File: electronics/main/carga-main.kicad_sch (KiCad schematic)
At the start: 74 parts, among them J1 USB2UART, J2 1.47 IPS LCD, J3 ConnBattery, J4 RTD_PT100, Q1 SS8050, Q2 SS8050, Q3 SS8050, SW1 RST, SW2 IN1, SW3 Boot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

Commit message: feat: add voltage regulator to carga main
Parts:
- removed C12, C18, C19, C20: 100nF, Capacitor_SMD:C_0805_2012Metric_Pad1.18x1.45mm_HandSolder, symbol Device:C
- removed C13, C16, C17: 10uF, Capacitor_SMD:C_0805_2012Metric_Pad1.18x1.45mm_HandSolder, symbol Device:C
- removed C22, C23: 4.7uF, Capacitor_SMD:C_0805_2012Metric_Pad1.18x1.45mm_HandSolder, symbol Device:C
- removed D1: INDICATOR, LED_SMD:LED_1206_3216Metric_Pad1.42x1.75mm_HandSolder, symbol Device:LED
- removed D2: VDD, LED_SMD:LED_1206_3216Metric_Pad1.42x1.75mm_HandSolder, symbol Device:LED
- removed D4: red, LED_SMD:LED_0805_2012Metric_Pad1.15x1.40mm_HandSolder, symbol Device:LED
- removed J3: ConnBattery, Connector_PinHeader_2.54mm:PinHeader_1x03_P2.54mm_Vertical, symbol Connector_Generic:Conn_01x03
- removed J4: RTD_PT100, TerminalBlock_Phoenix:TerminalBlock_Phoenix_PT-1,5-3-5.0-H_1x03_P5.00mm_Horizontal, symbol Connector:Screw_Terminal_01x03
- removed JP1: 3_OR_2_Wire, Jumper:SolderJumper-3_P1.3mm_Open_RoundedPad1.0x1.5mm, symbol Jumper:SolderJumper_3_Open
- removed JP2: 2_Wire, Jumper:SolderJumper-2_P1.3mm_Open_TrianglePad1.0x1.5mm, symbol Jumper:SolderJumper_2_Open
- removed L1: 22uH 1A, Inductor_SMD:L_Bourns_SRP7028A_7.3x6.6mm, symbol Device:L
- removed Q3: SS8050, Package_TO_SOT_SMD:SOT-23_Handsoldering, symbol Transistor_BJT:BC817
- removed R13, R14: 1k, Resistor_SMD:R_0805_2012Metric_Pad1.20x1.40mm_HandSolder, symbol Device:R_US
- removed R15: 100, Resistor_SMD:R_0805_2012Metric_Pad1.20x1.40mm_HandSolder, symbol Device:R_US
- removed R16: 46.4K, Resistor_SMD:R_0805_2012Metric_Pad1.20x1.40mm_HandSolder, symbol Device:R_US
- removed R17: 2K2, Resistor_SMD:R_0805_2012Metric_Pad1.20x1.40mm_HandSolder, symbol Device:R_US
- removed R18: 1.13k, Resistor_SMD:R_0805_2012Metric_Pad1.20x1.40mm_HandSolder, symbol Device:R_US
- removed R19: 400 1%, Resistor_SMD:R_0805_2012Metric_Pad1.20x1.40mm_HandSolder, symbol Device:R_US
- removed R20, R21: 1K5, Resistor_SMD:R_0805_2012Metric_Pad1.20x1.40mm_HandSolder, symbol Device:R_US
- removed U3: TPS63001_SEPIC_3V3, Package_SON:Texas_DRC0010J_ThermalVias, symbol Regulator_Switching:TPS63001
- removed U4: MAX31865xTP, Package_DFN_QFN:TQFN-20-1EP_5x5mm_P0.65mm_EP3.25x3.25mm, symbol Sensor_Temperature:MAX31865xTP
- removed U5: BQ24075RGT_DPPM, Package_DFN_QFN:VQFN-16-1EP_3x3mm_P0.5mm_EP1.6x1.6mm, symbol Battery_Management:BQ24075RGT
- removed U6: HX711, Package_SO:SOIC-16_3.9x9.9mm_P1.27mm, symbol Analog_ADC:HX711
- added C12: 0.33uF, Capacitor_SMD:C_0805_2012Metric_Pad1.18x1.45mm_HandSolder, symbol Device:C_Polarized
- added C13: 0.1uF, Capacitor_SMD:C_0805_2012Metric_Pad1.18x1.45mm_HandSolder, symbol Device:C_Polarized
- added J12: PWRInput, TerminalBlock_Phoenix:TerminalBlock_Phoenix_PT-1,5-2-5.0-H_1x02_P5.00mm_Horizontal, symbol Connector:Screw_Terminal_01x02
- added J4: DriverConn2, Connector_IDC:IDC-Header_2x05_P2.54mm_Vertical, symbol Connector_Generic:Conn_02x05_Odd_Even
- added J5: DriverConn, Connector_IDC:IDC-Header_2x05_P2.54mm_Vertical, symbol Connector_Generic:Conn_02x05_Odd_Even
- added J6: SensorConn, Connector_IDC:IDC-Header_2x05_P2.54mm_Vertical, symbol Connector_Generic:Conn_02x05_Odd_Even
- added U3: L7805, Package_TO_SOT_THT:TO-220F-3_Horizontal_TabDown, symbol Regulator_Linear:L7805
- added U4: AMS1117-3.3, Package_TO_SOT_SMD:SOT-223-3_TabPin2, symbol Regulator_Linear:AMS1117-3.3
- C14: value 0.1uF -> 22uF
- C15: value 1uF -> 22uF
- D3: value green -> PWR; footprint LED_SMD:LED_0805_2012Metric_Pad1.15x1.40mm_HandSolder -> LED_SMD:LED_1206_3216Metric_Pad1.42x1.75mm_HandSolder
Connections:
- net ~{PGOOD} is gone; now on net GND: D3.1 (K)
- net +3.3V: now also C15.1, J5.1 (Pin_1), J6.1 (Pin_1), U4.2 (VO)
- net GND: now also C12.2, C13.2, J12.2 (Pin_2), J5.10 (Pin_10), J6.10 (Pin_10), U3.2 (GND), U4.1 (GND)
- net VBUS: no longer C15.1
- net at D3.2 (A): now also R8.2
- net +5V: now reaches R8.1
- net +5V: now also C14.1, C13.1, J5.2 (Pin_2), J6.2 (Pin_2), U3.3 (OUT), U4.3 (VI)
- net at U2.4 (IO4): no longer R8.2
- net IN_SOL_VIB: now reaches U2.16 (IO46)
- net IN_SOL_VIB: now also J4.7 (Pin_7)
- net IN_SOL_VIA: now reaches U2.26 (IO45)
- net IN_SOL_VIA: now also J4.5 (Pin_5)
- net IN_ENA1: now reaches U2.31 (IO38)
- net IN_ENA1: now also J5.3 (Pin_3)
- net IN_ENB1: now reaches U2.32 (IO39)
- net IN_ENB1: now also J5.5 (Pin_5)
- net IN_ENA2: now reaches U2.33 (IO40)
- net IN_ENA2: now also J5.7 (Pin_7)
- net IN_ENB2: now reaches U2.34 (IO41)
- net IN_ENB2: now also J5.9 (Pin_9)
- net IN_SERVO: now reaches U2.35 (IO42)
- net IN_SERVO: now also J4.3 (Pin_3)
- net PD_SCK: now reaches U2.38 (IO2)
- net PD_SCK: now also J6.6 (Pin_6)
- net DOUT: now reaches U2.39 (IO1)
- net DOUT: now also J6.4 (Pin_4)
- net I2C_SDA: now reaches U2.6 (IO6)
- net I2C_SDA: now also J5.6 (Pin_6)
- net I2C_SCK: now reaches U2.7 (IO7)
- net I2C_SCK: now also J5.8 (Pin_8)
- new net +12V: C12.1, J12.1 (Pin_1), U3.1 (IN)
- new net GNDA: J4.10 (Pin_10)
- new net GNDB: J4.8 (Pin_8)
- new net VDDA: J4.2 (Pin_2)
- new net VDDB: J4.4 (Pin_4)
- new net VM: J5.4 (Pin_4)
- new net VSER: J4.1 (Pin_1)
- no-connect marks 24 -> 11
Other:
- note removed: "3 Wire to Force+ 2/4 Wire to GND Connect 2_Wire if use 2/4 Wire"
- note removed: "DPPM"
- note removed: "Program Fast-Charge Safety Timer (TMR): RTMR = tMAXCHG / (10 × KTMR ) KTMR = 48 s/kΩ from the electrical characteristics table. RTMR = (6.25 hr × 3600 s/hr) / (10 × 48 s/kΩ) = 46.8 kΩ -> 46.4 kΩ"
- note removed: "Program the Fast Charge Current (ISET): RISET = KISET / ICHG KISET = 890 AΩ from the electrical characteristics table. RISET = 890 AΩ / 0.8 A = 1.1125 kΩ -> 1.13 kΩ"
- note removed: "SEPIC 3.3V"
- note removed: "dynamic power path management"
- title: (none) -> Carga Main Module
- moved on the sheet: C1, C10, C11, C2, C3, C4, C5, C6, C7, C8, C9, H1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

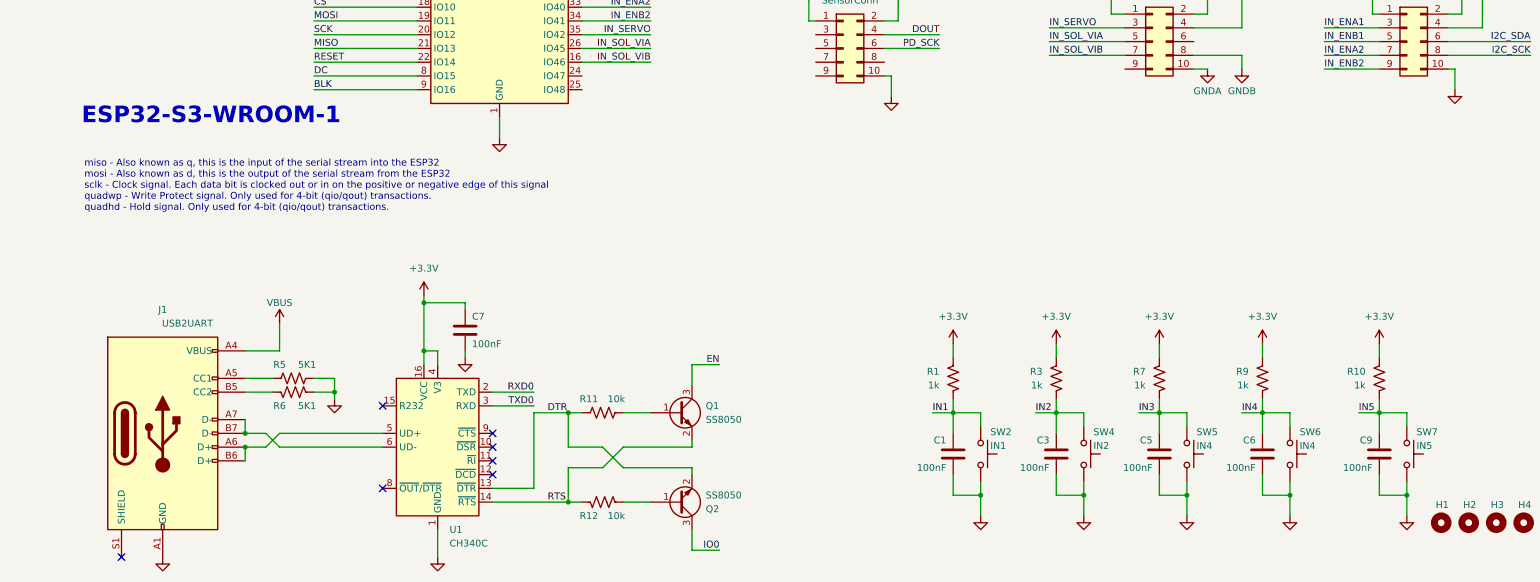
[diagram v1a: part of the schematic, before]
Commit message: feat: arrange component in carga main
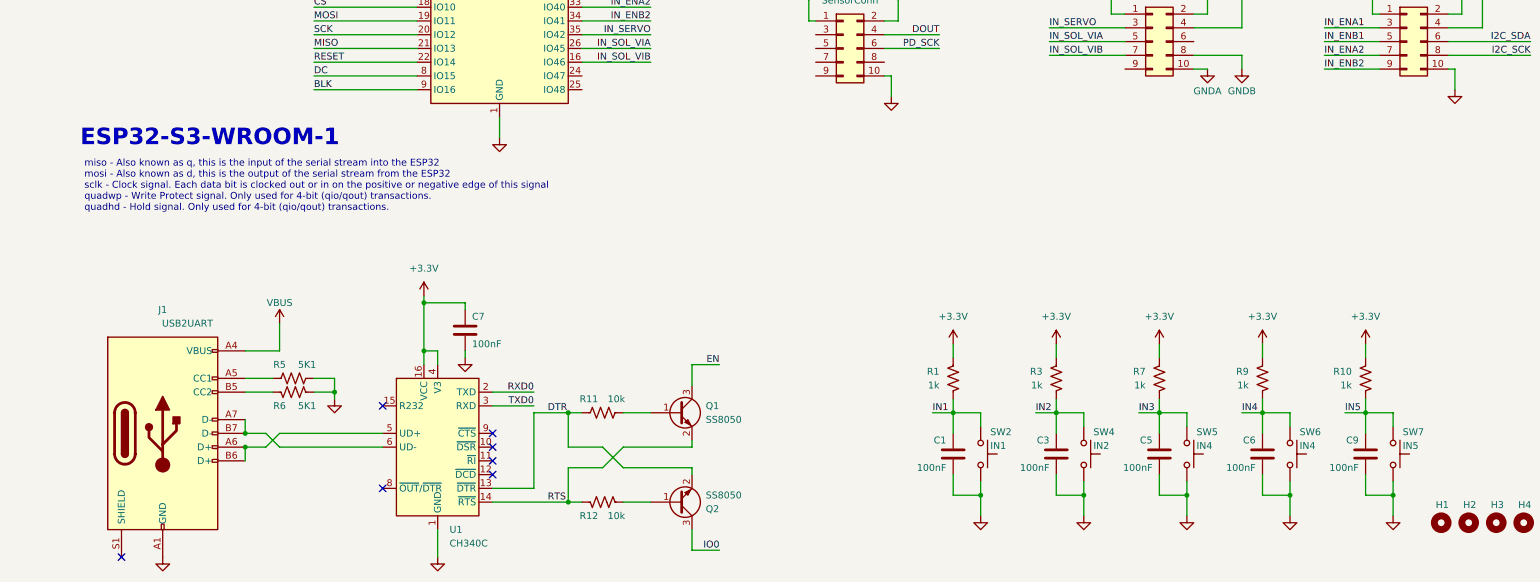
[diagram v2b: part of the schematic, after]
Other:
- moved on the sheet: C9, R10, SW7
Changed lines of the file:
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@@
 	(text "ESP32-S3-WROOM-1"
 		(exclude_from_sim no)
-		(at 14.224 85.598 0)
+		(at 13.97 89.662 0)
 		(effects
 			(font
@@
 	)
 	(junction
-		(at 254 142.24)
+		(at 251.46 142.24)
 		(diameter 0)
 		(color 0 0 0 0)
@@
 	)
 	(junction
-		(at 259.08 157.48)
+		(at 256.54 157.48)
 		(diameter 0)
 		(color 0 0 0 0)
@@
 	(wire
 		(pts
-			(xy 259.08 154.94) (xy 259.08 157.48)
+			(xy 256.54 154.94) (xy 256.54 157.48)
 		)
 		(stroke
@@
 	(wire
 		(pts
-			(xy 259.08 142.24) (xy 254 142.24)
+			(xy 256.54 142.24) (xy 251.46 142.24)
 		)
 		(stroke
@@
 	(wire
 		(pts
-			(xy 259.08 157.48) (xy 254 157.48)
+			(xy 256.54 157.48) (xy 251.46 157.48)
 		)
 		(stroke
@@
 	(wire
 		(pts
-			(xy 254 142.24) (xy 254 146.05)
+			(xy 251.46 142.24) (xy 251.46 146.05)
 		)
 		(stroke
@@
 	(wire
 		(pts
-			(xy 254 139.7) (xy 254 142.24)
+			(xy 251.46 139.7) (xy 251.46 142.24)
 		)
 		(stroke
@@
 	(wire
 		(pts
-			(xy 259.08 144.78) (xy 259.08 142.24)
+			(xy 256.54 144.78) (xy 256.54 142.24)
 		)
 		(stroke
@@
 	(wire
 		(pts
-			(xy 259.08 157.48) (xy 259.08 161.29)
+			(xy 256.54 157.48) (xy 256.54 161.29)
 		)
 		(stroke
@@
 	(wire
 		(pts
-			(xy 254 129.54) (xy 254 132.08)
+			(xy 251.46 129.54) (xy 251.46 132.08)
 		)
 		(stroke
@@
 	(wire
 		(pts
-			(xy 250.19 142.24) (xy 254 142.24)
+			(xy 247.65 142.24) (xy 251.46 142.24)
 		)
 		(stroke
@@
 	(wire
 		(pts
-			(xy 254 157.48) (xy 254 153.67)
+			(xy 251.46 157.48) (xy 251.46 153.67)
 		)
 		(stroke
@@
 	)
 	(label "IN5"
-		(at 250.19 142.24 0)
+		(at 247.65 142.24 0)
 		(effects
 			(font
@@
 	(symbol
 		(lib_id "Device:C")
-		(at 254 149.86 0)
+		(at 251.46 149.86 0)
 		(mirror y)
 		(unit 1)
@@
 		(dnp no)
 		(property "Reference" "C9"
-			(at 252.73 147.32 0)
+			(at 250.19 147.32 0)
 			(effects
 				(font
@@
 		)
 		(property "Value" "100nF"
-			(at 252.73 152.4 0)
+			(at 250.19 152.4 0)
 			(effects
 				(font
@@
 		)
 		(property "Footprint" "Capacitor_SMD:C_0805_2012Metric_Pad1.18x1.45mm_HandSolder"
-			(at 253.0348 153.67 0)
+			(at 250.4948 153.67 0)
 			(effects
 				(font
@@
 		)
 		(property "Datasheet" "~"
-			(at 254 149.86 0)
+			(at 251.46 149.86 0)
 			(effects
 				(font
@@
 		)
 		(property "Description" ""
-			(at 254 149.86 0)
+			(at 251.46 149.86 0)
 			(effects
 				(font
@@
 	(symbol
 		(lib_id "power:GND")
-		(at 259.08 161.29 0)
+		(at 256.54 161.29 0)
 		(mirror y)
 		(unit 1)
@@
 		(dnp no)
 		(property "Reference" "#PWR023"
-			(at 259.08 167.64 0)
+			(at 256.54 167.64 0)
 			(effects
 				(font
@@
 		)
 		(property "Value" "GND"
-			(at 261.62 163.83 0)
+			(at 259.08 163.83 0)
 			(effects
 				(font
@@
 		)
 		(property "Footprint" ""
-			(at 259.08 161.29 0)
+			(at 256.54 161.29 0)
 			(effects
 				(font
@@
 		)
 		(property "Datasheet" ""
-			(at 259.08 161.29 0)
+			(at 256.54 161.29 0)
 			(effects
 				(font
@@
 		)
 		(property "Description" ""
-			(at 259.08 161.29 0)
+			(at 256.54 161.29 0)
 			(effects
 				(font
@@
 		(on_board yes)
 		(dnp no)
-		(property "Reference" "#PWR025"
+		(property "Reference" "#PWR0101"
 			(at 222.25 85.09 0)
 			(effects
@@
 			(project "carga-main"
 				(path "/11d31181-5c23-445f-b117-2be40d0a6fe8"
-					(reference "#PWR025")
+					(reference "#PWR0101")
 					(unit 1)
 				)
@@
 		(dnp no)
 		(fields_autoplaced yes)
-		(property "Reference" "#PWR026"
+		(property "Reference" "#PWR0102"
 			(at 273.05 68.58 0)
 			(effects
@@
 			(project "carga-main"
 				(path "/11d31181-5c23-445f-b117-2be40d0a6fe8"
-					(reference "#PWR026")
+					(reference "#PWR0102")
 					(unit 1)
 				)
@@
 	(symbol
 		(lib_id "Switch:SW_Push")
-		(at 259.08 149.86 270)
+		(at 256.54 149.86 270)
 		(mirror x)
 		(unit 1)
@@
 		(dnp no)
 		(property "Reference" "SW7"
-			(at 260.858 145.796 90)
+			(at 258.318 145.796 90)
 			(effects
 				(font
@@
 		)
 		(property "Value" "IN5"
-			(at 260.858 148.336 90)
+			(at 258.318 148.336 90)
 			(effects
 				(font
@@
 		)
 		(property "Footprint" "Button_Switch_SMD:SW_SPST_Omron_B3FS-100xP"
-			(at 264.16 149.86 0)
+			(at 261.62 149.86 0)
 			(effects
 				(font
@@
 		)
 		(property "Datasheet" "~"
-			(at 264.16 149.86 0)
+			(at 261.62 149.86 0)
 			(effects
 				(font
@@
 		)
 		(property "Description" "Push button switch, generic, two pins"
-			(at 259.08 149.86 0)
+			(at 256.54 149.86 0)
 			(effects
 				(font
@@
 	(symbol
 		(lib_id "Device:R_US")
-		(at 254 135.89 0)
+		(at 251.46 135.89 0)
 		(mirror y)
 		(unit 1)
@@
 		(dnp no)
 		(property "Reference" "R10"
-			(at 251.46 134.6199 0)
+			(at 248.92 134.6199 0)
 			(effects
 				(font
@@
 		)
 		(property "Value" "1k"
-			(at 251.46 137.1599 0)
+			(at 248.92 137.1599 0)
 			(effects
 				(font
@@
 		)
 		(property "Footprint" "Resistor_SMD:R_0805_2012Metric_Pad1.20x1.40mm_HandSolder"
-			(at 252.984 136.144 90)
+			(at 250.444 136.144 90)
 			(effects
 				(font
@@
 		)
 		(property "Datasheet" "~"
-			(at 254 135.89 0)
+			(at 251.46 135.89 0)
 			(effects
 				(font
@@
 		)
 		(property "Description" ""
-			(at 254 135.89 0)
+			(at 251.46 135.89 0)
 			(effects
 				(font
@@
 	(symbol
 		(lib_id "power:+3.3V")
-		(at 254 129.54 0)
+		(at 251.46 129.54 0)
 		(mirror y)
 		(unit 1)
@@
 		(fields_autoplaced yes)
 		(property "Reference" "#PWR022"
-			(at 254 133.35 0)
+			(at 251.46 133.35 0)
 			(effects
 				(font
@@
 		)
 		(property "Value" "+3.3V"
-			(at 254 124.46 0)
+			(at 251.46 124.46 0)
 			(effects
 				(font
@@
 		)
 		(property "Footprint" ""
-			(at 254 129.54 0)
+			(at 251.46 129.54 0)
 			(effects
 				(font
@@
 		)
 		(property "Datasheet" ""
-			(at 254 129.54 0)
+			(at 251.46 129.54 0)
 			(effects
 				(font
@@
 		)
 		(property "Description" "Power symbol creates a global label with name \"+3.3V\""
-			(at 254 129.54 0)
+			(at 251.46 129.54 0)
 			(effects
 				(font
